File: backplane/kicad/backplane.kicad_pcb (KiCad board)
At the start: 4 copper layers, 140 x 67 mm, 15 parts, among them J1 Conn_01x02_Pin, J2 Conn_01x05_Pin

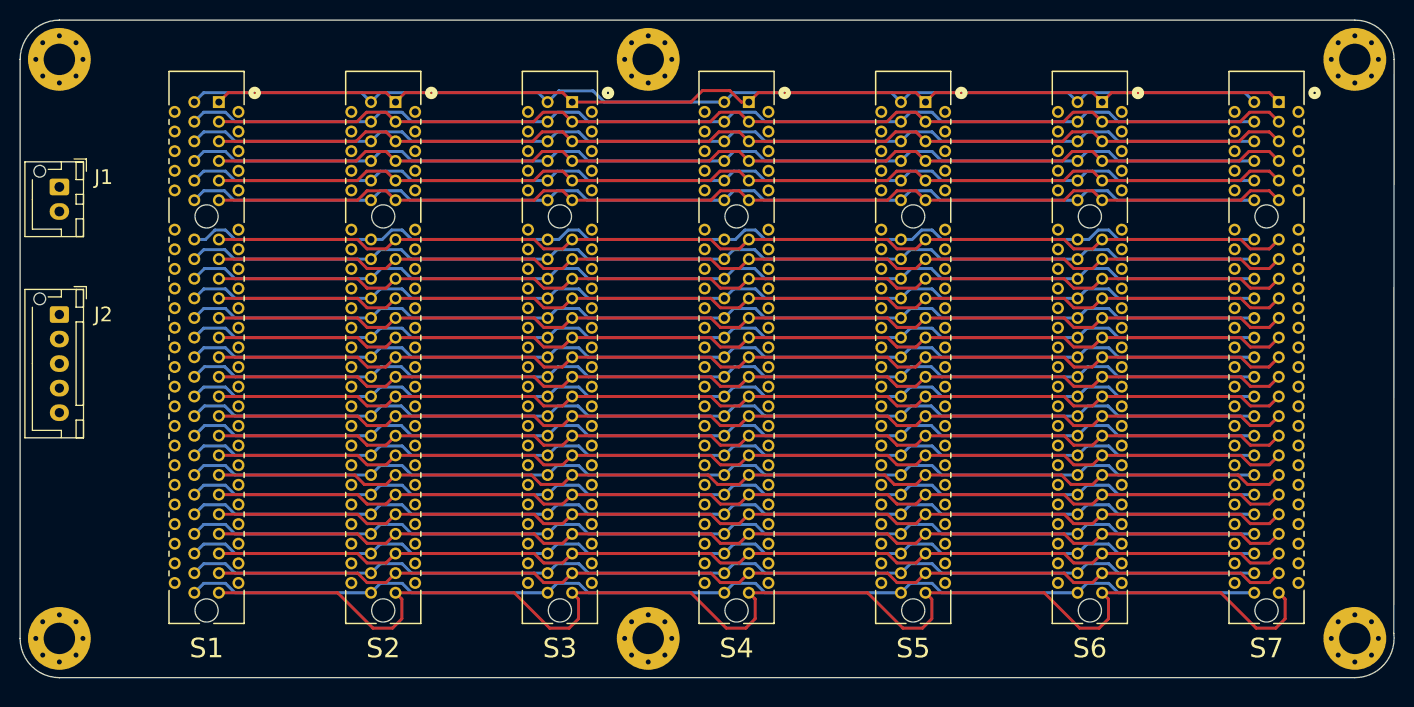
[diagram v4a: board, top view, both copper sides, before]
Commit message: Completed the routing of the backplane.
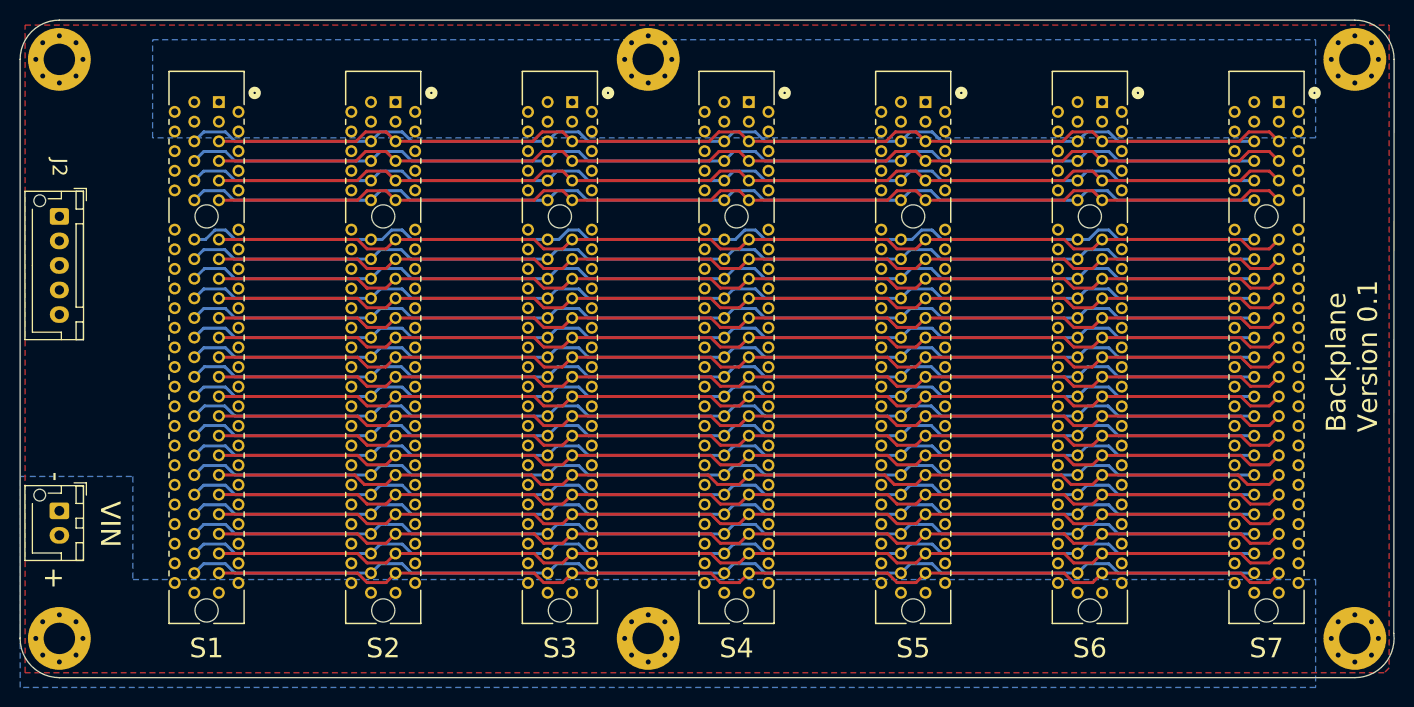
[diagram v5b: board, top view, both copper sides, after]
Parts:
- moved J1 33.0 mm to (85.0, 120.0)
- moved J2 10.0 mm to (85.0, 90.0)
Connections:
- J1 pad 1: unconnected-(J1-Pin_1-Pad1) -> /VIN-
- J1 pad 2: unconnected-(J1-Pin_2-Pad2) -> /VIN+
- S1 pad A1: /A1 -> /GND
- S1 pad A2: /A2 -> /GND
- S1 pad A3: /A3 -> /GND
- S1 pad A4: /A4 -> /GND
- S1 pad A48: /A48 -> /VIN-
- S1 pad A49: /A49 -> /VIN-
- S1 pad B1: /B1 -> /+5V
- S1 pad B2: /B2 -> /+5V
- S1 pad B3: /B3 -> /+5V
- S1 pad B4: /B4 -> /+5V
- S1 pad B48: /B48 -> /VIN+
- S1 pad B49: /B49 -> /VIN+
- S2 pad A1: /A1 -> /GND
- S2 pad A2: /A2 -> /GND
- S2 pad A3: /A3 -> /GND
- S2 pad A4: /A4 -> /GND
- S2 pad A48: /A48 -> /VIN-
- S2 pad A49: /A49 -> /VIN-
- S2 pad B1: /B1 -> /+5V
- S2 pad B2: /B2 -> /+5V
- S2 pad B3: /B3 -> /+5V
- S2 pad B4: /B4 -> /+5V
- S2 pad B48: /B48 -> /VIN+
- S2 pad B49: /B49 -> /VIN+
- S3 pad A1: /A1 -> /GND
- S3 pad A2: /A2 -> /GND
- S3 pad A3: /A3 -> /GND
- S3 pad A4: /A4 -> /GND
- S3 pad A48: /A48 -> /VIN-
- S3 pad A49: /A49 -> /VIN-
- S3 pad B1: /B1 -> /+5V
- S3 pad B2: /B2 -> /+5V
- S3 pad B3: /B3 -> /+5V
- S3 pad B4: /B4 -> /+5V
- S3 pad B48: /B48 -> /VIN+
- S3 pad B49: /B49 -> /VIN+
- S4 pad A1: /A1 -> /GND
- S4 pad A2: /A2 -> /GND
- S4 pad A3: /A3 -> /GND
- S4 pad A4: /A4 -> /GND
- S4 pad A48: /A48 -> /VIN-
- S4 pad A49: /A49 -> /VIN-
- S4 pad B1: /B1 -> /+5V
- S4 pad B2: /B2 -> /+5V
- S4 pad B3: /B3 -> /+5V
- S4 pad B4: /B4 -> /+5V
- S4 pad B48: /B48 -> /VIN+
- S4 pad B49: /B49 -> /VIN+
- S5 pad A1: /A1 -> /GND
- S5 pad A2: /A2 -> /GND
- S5 pad A3: /A3 -> /GND
- S5 pad A4: /A4 -> /GND
- S5 pad A48: /A48 -> /VIN-
- S5 pad A49: /A49 -> /VIN-
- S5 pad B1: /B1 -> /+5V
- S5 pad B2: /B2 -> /+5V
- S5 pad B3: /B3 -> /+5V
- S5 pad B4: /B4 -> /+5V
- S5 pad B48: /B48 -> /VIN+
- S5 pad B49: /B49 -> /VIN+
- S6 pad A1: /A1 -> /GND
- S6 pad A2: /A2 -> /GND
- S6 pad A3: /A3 -> /GND
- S6 pad A4: /A4 -> /GND
- S6 pad A48: /A48 -> /VIN-
- S6 pad A49: /A49 -> /VIN-
- S6 pad B1: /B1 -> /+5V
- S6 pad B2: /B2 -> /+5V
- S6 pad B3: /B3 -> /+5V
- S6 pad B4: /B4 -> /+5V
- S6 pad B48: /B48 -> /VIN+
- S6 pad B49: /B49 -> /VIN+
- S7 pad A1: /A1 -> /GND
- S7 pad A2: /A2 -> /GND
- S7 pad A3: /A3 -> /GND
- S7 pad A4: /A4 -> /GND
- S7 pad A48: /A48 -> /VIN-
- S7 pad A49: /A49 -> /VIN-
- S7 pad B1: /B1 -> /+5V
- S7 pad B2: /B2 -> /+5V
- S7 pad B3: /B3 -> /+5V
- S7 pad B4: /B4 -> /+5V
- S7 pad B48: /B48 -> /VIN+
- S7 pad B49: /B49 -> /VIN+
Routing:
- net /A49: track 140.7 -> 0.00 mm
- net /A48: track 139.3 -> 0.00 mm
- net /B48: track 139.1 -> 0.00 mm
- net /B2: track 120.4 -> 0.00 mm
- net /A1: track 113.0 -> 0.00 mm
- net /B1: track 112.9 -> 0.00 mm
- net /A4: track 112.8 -> 0.00 mm
- net /B3: track 112.8 -> 0.00 mm
- net /B49: track 112.8 -> 0.00 mm
- net /B4: track 112.8 -> 0.00 mm
- net /A3: track 112.8 -> 0.00 mm
- net /A2: track 112.8 -> 0.00 mm
- added copper zone on In1.Cu, net /+5V
- added copper zone on In2.Cu, net /+5V
- added copper zone on B.Cu, net /GND
- added copper zone on F.Cu, net /GND
- added copper zone on In2.Cu, net /VIN+
- added copper zone on B.Cu, net /VIN-
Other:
- board text added: "+"
- board text added: "-"
- board text added: "Backplane Version 0.1"
- board text added: "VIN"

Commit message: Removed the backplane 5pins connector.
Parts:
- removed J2: Conn_01x05_Pin, backplane:JST_XH_B5B-XH-AM_1x05_P2.50mm_Vertical
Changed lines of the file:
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@@
   (net 89 "/B46")
   (net 90 "/B47")
-  (net 91 "unconnected-(J2-Pin_1-Pad1)")
-  (net 92 "unconnected-(J2-Pin_5-Pad5)")
-  (net 93 "unconnected-(J2-Pin_4-Pad4)")
-  (net 94 "unconnected-(J2-Pin_3-Pad3)")
-  (net 95 "unconnected-(J2-Pin_2-Pad2)")
   (footprint "backplane:pcie_98_socket" locked (layer "F.Cu")
     (at 136 90 -90)
@@
     (pad "1" thru_hole circle locked (at 2.4 0) (size 0.8 0.8) (drill 0.5) (layers "*.Cu" "*.Mask"))
   )
-  (footprint "backplane:JST_XH_B5B-XH-AM_1x05_P2.50mm_Vertical" (layer "F.Cu")
-    (at 85 90 -90)
-    (descr "JST XH series connector, B5B-XH-AM, with boss (http://www.jst-mfg.com/product/pdf/eng/eXH.pdf), generated with kicad-footprint-generator")
-    (tags "connector JST XH vertical boss")
-    (property "Sheetfile" "backplane.kicad_sch")
-    (property "Sheetname" "")
-    (property "ki_description" "Generic connector, single row, 01x05, script generated (kicad-library-utils/schlib/autogen/connector/)")
-    (property "ki_keywords" "connector")
-    (attr through_hole)
-    (fp_text reference "J2" (at -5 0 -90 unlocked) (layer "F.SilkS")
-        (effects (font (size 1.5 1.5) (thickness 0.22)))
-    )
-    (fp_text value "Conn_01x05_Pin" (at 5 4.6 90) (layer "F.Fab") hide
-        (effects (font (size 1 1) (thickness 0.15)))
-    )
-    (fp_text user "${REFERENCE}" (at 5 2.7 90) (layer "F.Fab") hide
-        (effects (font (size 1 1) (thickness 0.15)))
-    )
-    (fp_line (start -2.85 -2.75) (end -2.85 -1.5)
-      (stroke (width 0.12) (type solid)) (layer "F.SilkS"))
-    (fp_line (start -2.56 -2.46) (end -2.56 3.51)
-      (stroke (width 0.12) (type solid)) (layer "F.SilkS"))
-    (fp_line (start -2.56 3.51) (end 12.56 3.51)
-      (stroke (width 0.12) (type solid)) (layer "F.SilkS"))
-    (fp_line (start -2.55 -2.45) (end -2.55 -1.7)
-      (stroke (width 0.12) (type solid)) (layer "F.SilkS"))
-    (fp_line (start -2.55 -1.7) (end -0.75 -1.7)
-      (stroke (width 0.12) (type solid)) (layer "F.SilkS"))
-    (fp_line (start -2.55 -0.2) (end -1.8 -0.2)
-      (stroke (width 0.12) (type solid)) (layer "F.SilkS"))
-    (fp_line (start -1.8 -0.2) (end -1.8 1.14)
-      (stroke (width 0.12) (type solid)) (layer "F.SilkS"))
-    (fp_line (start -1.6 -2.75) (end -2.85 -2.75)
-      (stroke (width 0.12) (type solid)) (layer "F.SilkS"))
-    (fp_line (start -0.75 -2.45) (end -2.55 -2.45)
-      (stroke (width 0.12) (type solid)) (layer "F.SilkS"))
-    (fp_line (start -0.75 -1.7) (end -0.75 -2.45)
-      (stroke (width 0.12) (type solid)) (layer "F.SilkS"))
-    (fp_line (start 0.75 -2.45) (end 0.75 -1.7)
-      (stroke (width 0.12) (type solid)) (layer "F.SilkS"))
-    (fp_line (start 0.75 -1.7) (end 9.25 -1.7)
-      (stroke (width 0.12) (type solid)) (layer "F.SilkS"))
-    (fp_line (start 5 2.75) (end -0.74 2.75)
-      (stroke (width 0.12) (type solid)) (layer "F.SilkS"))
-    (fp_line (start 9.25 -2.45) (end 0.75 -2.45)
-      (stroke (width 0.12) (type solid)) (layer "F.SilkS"))
-    (fp_line (start 9.25 -1.7) (end 9.25 -2.45)
-      (stroke (width 0.12) (type solid)) (layer "F.SilkS"))
-    (fp_line (start 10.75 -2.45) (end 10.75 -1.7)
-      (stroke (width 0.12) (type solid)) (layer "F.SilkS"))
-    (fp_line (start 10.75 -1.7) (end 12.55 -1.7)
-      (stroke (width 0.12) (type solid)) (layer "F.SilkS"))
-    (fp_line (start 11.8 -0.2) (end 11.8 2.75)
-      (stroke (width 0.12) (type solid)) (layer "F.SilkS"))
-    (fp_line (start 11.8 2.75) (end 5 2.75)
-      (stroke (width 0.12) (type solid)) (layer "F.SilkS"))
-    (fp_line (start 12.55 -2.45) (end 10.75 -2.45)
-      (stroke (width 0.12) (type solid)) (layer "F.SilkS"))
-    (fp_line (start 12.55 -1.7) (end 12.55 -2.45)
-      (stroke (width 0.12) (type solid)) (layer "F.SilkS"))
-    (fp_line (start 12.55 -0.2) (end 11.8 -0.2)
-      (stroke (width 0.12) (type solid)) (layer "F.SilkS"))
-    (fp_line (start 12.56 -2.46) (end -2.56 -2.46)
-      (stroke (width 0.12) (type solid)) (layer "F.SilkS"))
-    (fp_line (start 12.56 3.51) (end 12.56 -2.46)
-      (stroke (width 0.12) (type solid)) (layer "F.SilkS"))
-    (fp_line (start -2.95 -2.85) (end -2.95 3.9)
-      (stroke (width 0.05) (type solid)) (layer "F.CrtYd"))
-    (fp_line (start -2.95 3.9) (end 12.95 3.9)
-      (stroke (width 0.05) (type solid)) (layer "F.CrtYd"))
-    (fp_line (start 12.95 -2.85) (end -2.95 -2.85)
-      (stroke (width 0.05) (type solid)) (layer "F.CrtYd"))
-    (fp_line (start 12.95 3.9) (end 12.95 -2.85)
-      (stroke (width 0.05) (type solid)) (layer "F.CrtYd"))
-    (fp_line (start -2.45 -2.35) (end -2.45 3.4)
-      (stroke (width 0.1) (type solid)) (layer "F.Fab"))
-    (fp_line (start -2.45 3.4) (end 12.45 3.4)
-      (stroke (width 0.1) (type solid)) (layer "F.Fab"))
-    (fp_line (start -0.625 -2.35) (end 0 -1.35)
-      (stroke (width 0.1) (type solid)) (layer "F.Fab"))
-    (fp_line (start 0 -1.35) (end 0.625 -2.35)
-      (stroke (width 0.1) (type solid)) (layer "F.Fab"))
-    (fp_line (start 12.45 -2.35) (end -2.45 -2.35)
-      (stroke (width 0.1) (type solid)) (layer "F.Fab"))
-    (fp_line (start 12.45 3.4) (end 12.45 -2.35)
-      (stroke (width 0.1) (type solid)) (layer "F.Fab"))
-    (pad "" np_thru_hole circle (at -1.6 2 270) (size 1.2 1.2) (drill 1.2) (layers "*.Cu" "*.Mask"))
-    (pad "1" thru_hole roundrect (at 0 0 270) (size 1.7 1.95) (drill 0.95) (layers "*.Cu" "*.Mask") (roundrect_rratio 0.147059)
-      (net 91 "unconnected-(J2-Pin_1-Pad1)") (pinfunction "Pin_1") (pintype "passive+no_connect"))
-    (pad "2" thru_hole oval (at 2.5 0 270) (size 1.7 1.95) (drill 0.95) (layers "*.Cu" "*.Mask")
-      (net 95 "unconnected-(J2-Pin_2-Pad2)") (pinfunction "Pin_2") (pintype "passive+no_connect"))
-    (pad "3" thru_hole oval (at 5 0 270) (size 1.7 1.95) (drill 0.95) (layers "*.Cu" "*.Mask")
-      (net 94 "unconnected-(J2-Pin_3-Pad3)") (pinfunction "Pin_3") (pintype "passive+no_connect"))
-    (pad "4" thru_hole oval (at 7.5 0 270) (size 1.7 1.95) (drill 0.95) (layers "*.Cu" "*.Mask")
-      (net 93 "unconnected-(J2-Pin_4-Pad4)") (pinfunction "Pin_4") (pintype "passive+no_connect"))
-    (pad "5" thru_hole oval (at 10 0 270) (size 1.7 1.95) (drill 0.95) (layers "*.Cu" "*.Mask")
-      (net 92 "unconnected-(J2-Pin_5-Pad5)") (pinfunction "Pin_5") (pintype "passive+no_connect"))
-    (model "${KICAD7_3DMODEL_DIR}/Connector_JST.3dshapes/JST_XH_B5B-XH-A_1x05_P2.50mm_Vertical.step"
-      (offset (xyz 0 0 0))
-      (scale (xyz 1 1 1))
-      (rotate (xyz 0 0 0))
-    )
-  )
   (footprint "backplane:pcie_98_socket" locked (layer "F.Cu")
